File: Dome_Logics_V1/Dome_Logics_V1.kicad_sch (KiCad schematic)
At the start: 26 parts, among them J1 USB_B_Micro, J12 SERIAL_FU, J2 Conn_01x04, J3 Front Logics, J5 12OUT, J7 5V OUT, SW1 SW_Push, U1 ESP32-WROOM-32D_16MB_, U2 CJ2301_S1, U3 ME6211C33M5G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

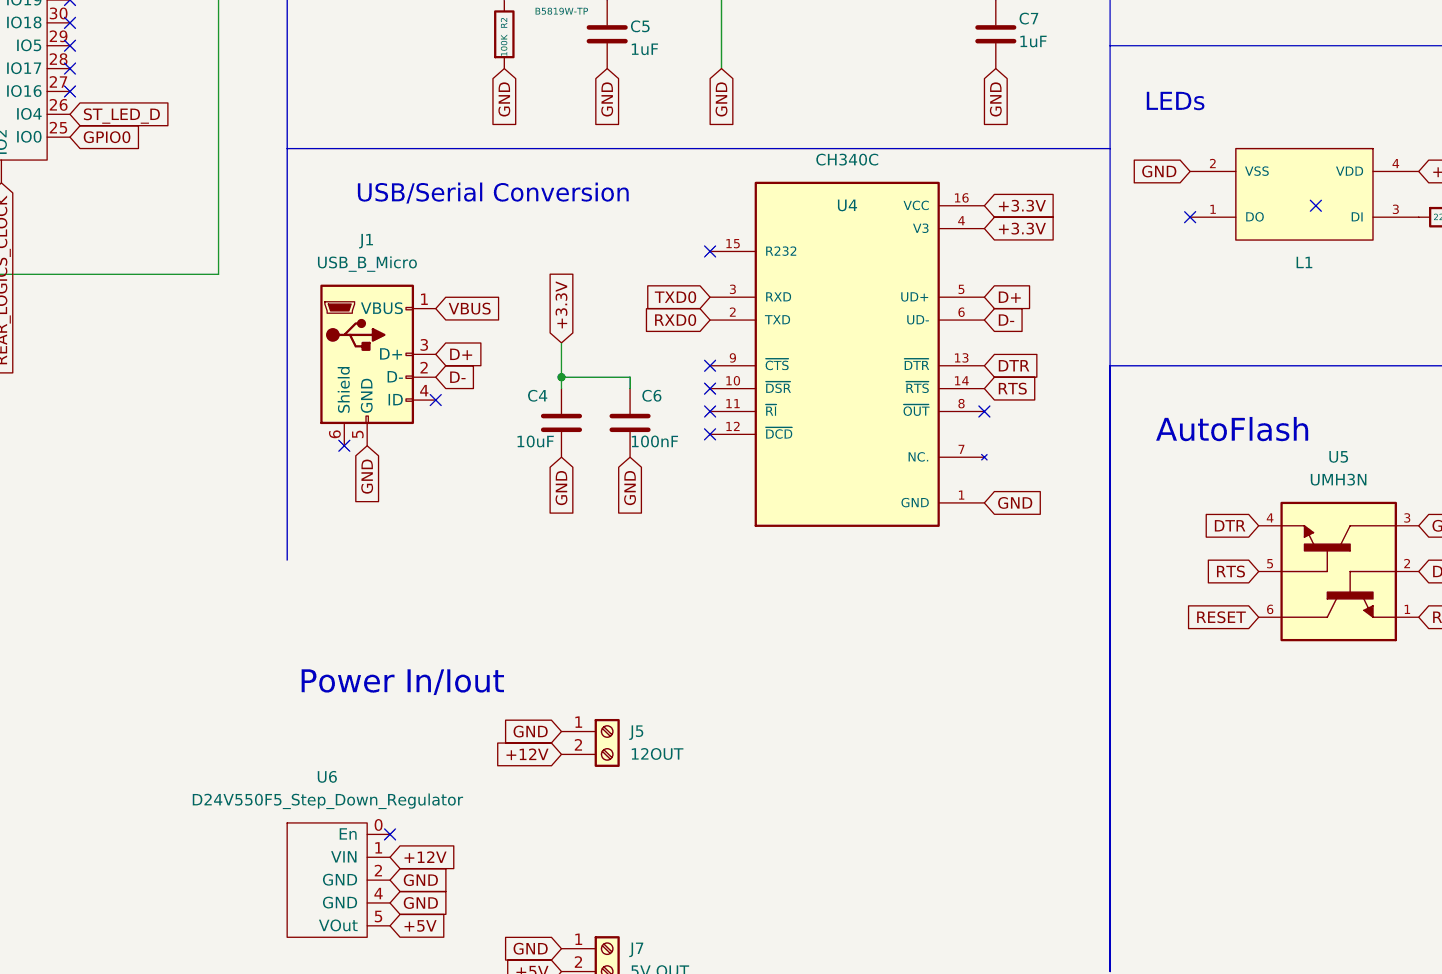
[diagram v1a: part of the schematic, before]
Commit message: added LED PCBs
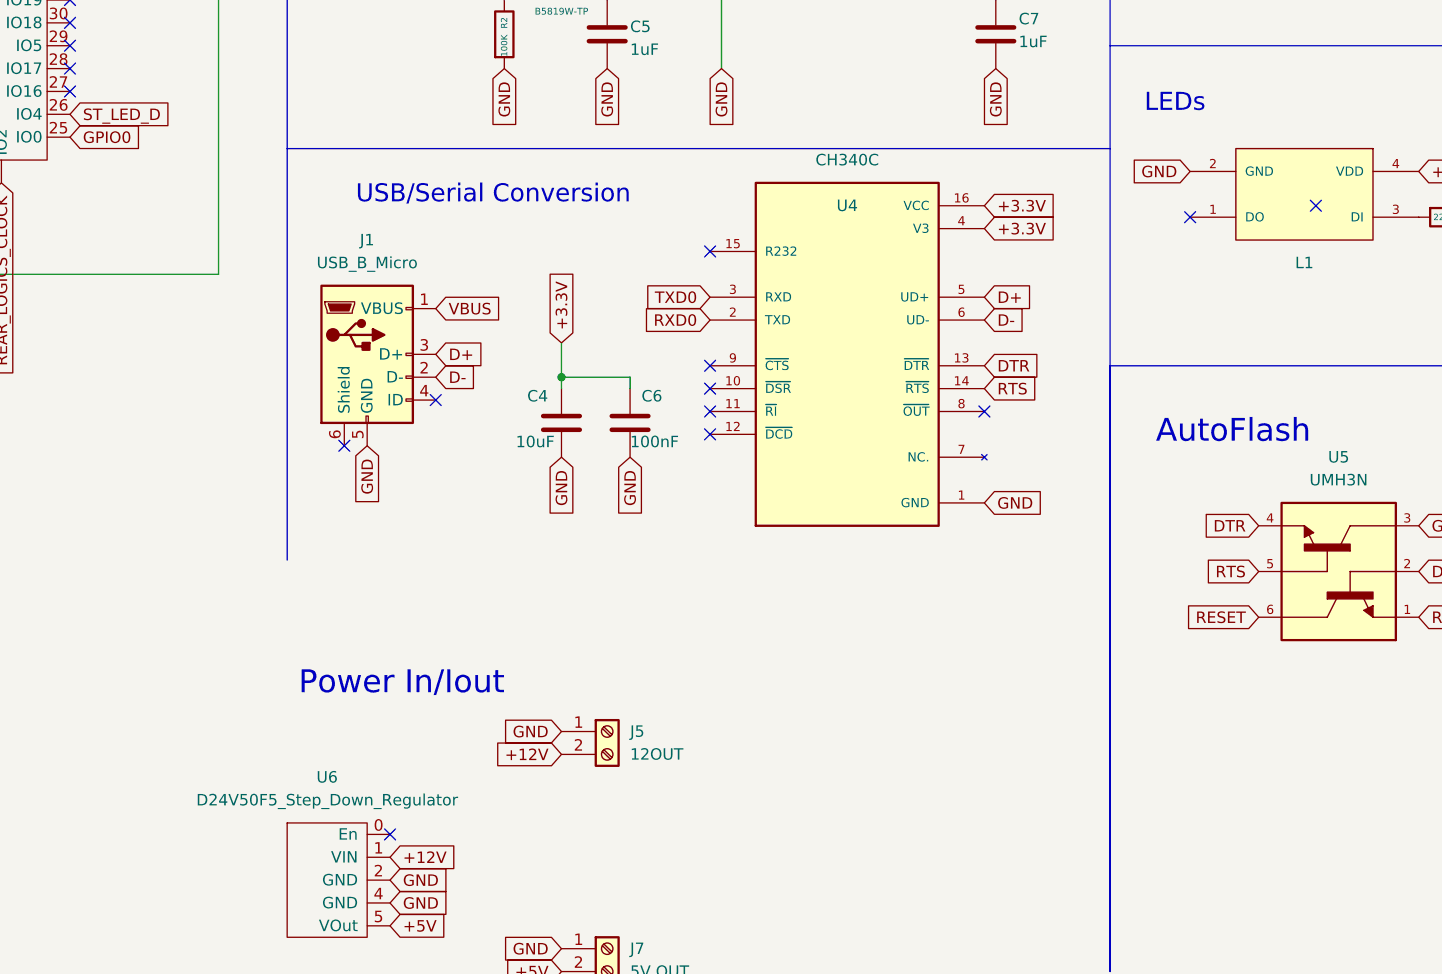
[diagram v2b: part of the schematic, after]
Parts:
- J2: LCSC (none) -> C240840
- L1: footprint Custom:WS2812B-2020 -> WS2812B-2020
- U6: value D24V550F5_Step_Down_Regulator -> D24V50F5_Step_Down_Regulator
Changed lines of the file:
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@@
       (effects (font (size 1.27 1.27)) hide)
     )
-    (property "Datasheet" "~" (id 3) (at 154.94 158.75 0)
+    (property "Datasheet" "https://datasheet.lcsc.com/lcsc/2001160007_Cixi-Kefa-Elec-KF350-3-5-2P_C474892.pdf" (id 3) (at 154.94 158.75 0)
       (effects (font (size 1.27 1.27)) hide)
     )
@@
       (effects (font (size 1.27 1.27)) hide)
     )
-    (property "Datasheet" "" (id 3) (at 181.61 55.88 0)
+    (property "Datasheet" "https://datasheet.lcsc.com/lcsc/1811131510_MICRONE-Nanjing-Micro-One-Elec-ME6211C33M5G-N_C82942.pdf" (id 3) (at 181.61 55.88 0)
       (effects (font (size 1.27 1.27)) hide)
     )
@@
       (effects (font (size 1.27 1.27)) hide)
     )
-    (property "Datasheet" "" (id 3) (at 74.93 53.34 0)
+    (property "Datasheet" "https://datasheet.lcsc.com/lcsc/2005211207_Espressif-Systems-ESP32-WROOM-32D-N16_C529578.pdf" (id 3) (at 74.93 53.34 0)
       (effects (font (size 1.27 1.27)) hide)
     )
@@
       (effects (font (size 1.27 1.27)) hide)
     )
-    (property "Datasheet" "~" (id 3) (at 154.94 134.62 0)
+    (property "Datasheet" "https://datasheet.lcsc.com/lcsc/2001160007_Cixi-Kefa-Elec-KF350-3-5-2P_C474892.pdf" (id 3) (at 154.94 134.62 0)
       (effects (font (size 1.27 1.27)) hide)
     )
@@
       (effects (font (size 1.27 1.27)) hide)
     )
-    (property "Datasheet" "" (id 3) (at 139.7 41.91 0)
+    (property "Datasheet" "https://datasheet.lcsc.com/lcsc/1809141711_Jiangsu-Changjing-Electronics-Technology-Co---Ltd--CJ2301-S1_C8547.pdf" (id 3) (at 139.7 41.91 0)
       (effects (font (size 1.27 1.27)) hide)
     )
@@
       (effects (font (size 1.27 1.27)) hide)
     )
-    (property "Datasheet" "~" (id 3) (at 132.08 93.98 0)
+    (property "Datasheet" "https://datasheet.lcsc.com/lcsc/1811131822_Amphenol-ICC-10118194-0001LF_C132563.pdf" (id 3) (at 132.08 93.98 0)
       (effects (font (size 1.27 1.27)) hide)
     )
@@
       (effects (font (size 1.27 1.27)) hide)
     )
-    (property "Datasheet" "~" (id 3) (at 154.94 57.15 0)
+    (property "Datasheet" "https://datasheet.lcsc.com/lcsc/1811081616_Murata-Electronics-GRM155R61E105KA12D_C77009.pdf" (id 3) (at 154.94 57.15 0)
       (effects (font (size 1.27 1.27)) hide)
     )
@@
       (effects (font (size 1.27 1.27)) hide)
     )
-    (property "Datasheet" "~" (id 3) (at 241.3 34.29 0)
+    (property "Datasheet" "https://datasheet.lcsc.com/lcsc/1811051309_MOLEX-470531000_C240840.pdf" (id 3) (at 241.3 34.29 0)
+      (effects (font (size 1.27 1.27)) hide)
+    )
+    (property "LCSC" "C240840" (id 4) (at 241.3 34.29 0)
       (effects (font (size 1.27 1.27)) hide)
     )
@@
       (effects (font (size 1.27 1.27)) hide)
     )
-    (property "Datasheet" "~" (id 3) (at 40.64 86.36 0)
+    (property "Datasheet" "https://datasheet.lcsc.com/lcsc/1810191222_Samsung-Electro-Mechanics-CL05B104KB54PNC_C307331.pdf" (id 3) (at 40.64 86.36 0)
       (effects (font (size 1.27 1.27)) hide)
     )
@@
       (effects (font (size 1.27 1.27)) (justify left bottom) hide)
     )
-    (property "Footprint" "Custom:WS2812B-2020" (id 2) (at 232.41 74.93 0)
-      (effects (font (size 1.27 1.27)) (justify left bottom) hide)
-    )
-    (property "Datasheet" "" (id 3) (at 232.41 74.93 0)
+    (property "Footprint" "WS2812B-2020" (id 2) (at 232.41 74.93 0)
+      (effects (font (size 1.27 1.27)) (justify left bottom) hide)
+    )
+    (property "Datasheet" "https://datasheet.lcsc.com/lcsc/2012110135_Worldsemi-WS2812B-2020_C965555.pdf" (id 3) (at 232.41 74.93 0)
       (effects (font (size 1.27 1.27)) (justify left bottom) hide)
     )
@@
       (effects (font (size 1.27 1.27)) hide)
     )
-    (property "Datasheet" "~" (id 3) (at 157.48 100.33 0)
+    (property "Datasheet" "https://datasheet.lcsc.com/lcsc/1810191222_Samsung-Electro-Mechanics-CL05B104KB54PNC_C307331.pdf" (id 3) (at 157.48 100.33 0)
       (effects (font (size 1.27 1.27)) hide)
     )
@@
       (effects (font (size 1.27 1.27)) hide)
     )
-    (property "Datasheet" "~" (id 3) (at 266.7 46.99 0)
+    (property "Datasheet" "https://datasheet.lcsc.com/lcsc/1912230932_MOLEX-22272031_C471416.pdf" (id 3) (at 266.7 46.99 0)
       (effects (font (size 1.27 1.27)) hide)
     )
@@
       (effects (font (size 1.27 1.27)) hide)
     )
-    (property "Datasheet" "~" (id 3) (at 198.12 57.15 0)
+    (property "Datasheet" "https://datasheet.lcsc.com/lcsc/1811081616_Murata-Electronics-GRM155R61E105KA12D_C77009.pdf" (id 3) (at 198.12 57.15 0)
       (effects (font (size 1.27 1.27)) hide)
     )
@@
       (effects (font (size 1.27 1.27)) (justify left bottom) hide)
     )
-    (property "Datasheet" "" (id 3) (at 234.95 111.76 0)
+    (property "Datasheet" "https://datasheet.lcsc.com/lcsc/1809211024_Jiangsu-Changjing-Electronics-Technology-Co---Ltd--UMH3N_C62892.pdf" (id 3) (at 234.95 111.76 0)
       (effects (font (size 1.27 1.27)) (justify left bottom) hide)
     )
@@
       (effects (font (size 1.27 1.27)) hide)
     )
-    (property "Datasheet" "~" (id 3) (at 143.51 57.15 0)
+    (property "Datasheet" "https://datasheet.lcsc.com/lcsc/2206010045_UNI-ROYAL-Uniroyal-Elec-0603WAF1003T5E_C25803.pdf" (id 3) (at 143.51 57.15 0)
       (effects (font (size 1.27 1.27)) hide)
     )
@@
     (in_bom yes) (on_board yes) (fields_autoplaced)
     (property "Reference" "U6" (id 0) (at 123.825 139.7 0))
-    (property "Value" "D24V550F5_Step_Down_Regulator" (id 1) (at 123.825 142.24 0))
+    (property "Value" "D24V50F5_Step_Down_Regulator" (id 1) (at 123.825 142.24 0))
     (property "Footprint" "Pololu:VoltageREG_2851" (id 2) (at 124.46 151.13 0)
       (effects (font (size 1.27 1.27)) hide)
     )
-    (property "Datasheet" "" (id 3) (at 124.46 151.13 0)
+    (property "Datasheet" "https://www.pololu.com/product/2851/specs" (id 3) (at 124.46 151.13 0)
       (effects (font (size 1.27 1.27)) hide)
     )
@@
       (effects (font (size 1.27 1.27)) hide)
     )
-    (property "Datasheet" "~" (id 3) (at 267.97 27.94 0)
+    (property "Datasheet" "https://datasheet.lcsc.com/lcsc/1912230932_MOLEX-22272031_C471416.pdf" (id 3) (at 267.97 27.94 0)
       (effects (font (size 1.27 1.27)) hide)
     )
@@
       (effects (font (size 1.27 1.27)) hide)
     )
-    (property "Datasheet" "~" (id 3) (at 33.02 50.8 0)
+    (property "Datasheet" "https://datasheet.lcsc.com/lcsc/2110111130_XKB-Connectivity-TS-1101S-B-B-B-W-A_C692465.pdf" (id 3) (at 33.02 50.8 0)
       (effects (font (size 1.27 1.27)) hide)
     )
@@
       (effects (font (size 1.27 1.27)) hide)
     )
-    (property "Datasheet" "~" (id 3) (at 31.75 86.36 0)
+    (property "Datasheet" "https://datasheet.lcsc.com/lcsc/2007131004_Samsung-Electro-Mechanics-CL05A106MP5NUNC_C315248.pdf" (id 3) (at 31.75 86.36 0)
       (effects (font (size 1.27 1.27)) hide)
     )
@@
       (effects (font (size 1.27 1.27)) hide)
     )
-    (property "Datasheet" "~" (id 3) (at 26.67 52.07 0)
+    (property "Datasheet" "https://datasheet.lcsc.com/lcsc/1810191222_Samsung-Electro-Mechanics-CL05B104KB54PNC_C307331.pdf" (id 3) (at 26.67 52.07 0)
       (effects (font (size 1.27 1.27)) hide)
     )
@@
       (effects (font (size 1.27 1.27)) hide)
     )
-    (property "Datasheet" "~" (id 3) (at 38.1 34.29 0)
+    (property "Datasheet" "https://datasheet.lcsc.com/lcsc/1811101830_TyoHM-RMC-0603-10K-F-N_C269701.pdf" (id 3) (at 38.1 34.29 0)
       (effects (font (size 1.27 1.27)) hide)
     )
@@
       (effects (font (size 1.524 1.524)) hide)
     )
-    (property "Datasheet" "" (id 3) (at 144.78 50.8 0)
-      (effects (font (size 1.524 1.524)))
+    (property "Datasheet" "https://datasheet.lcsc.com/lcsc/1810010311_MCC-Micro-Commercial-Components-B5819W-TP_C84354.pdf" (id 3) (at 144.78 50.8 0)
+      (effects (font (size 1.524 1.524)) hide)
     )
     (property "LCSC" "C84354" (id 4) (at 144.78 50.8 0)
@@
       (effects (font (size 1.27 1.27)) hide)
     )
-    (property "Datasheet" "~" (id 3) (at 162.56 48.26 0)
+    (property "Datasheet" "https://datasheet.lcsc.com/lcsc/2206010045_UNI-ROYAL-Uniroyal-Elec-0603WAF1003T5E_C25803.pdf" (id 3) (at 162.56 48.26 0)
       (effects (font (size 1.27 1.27)) hide)
     )
@@
       (effects (font (size 1.27 1.27)) (justify left bottom) hide)
     )
-    (property "Datasheet" "" (id 3) (at 181.61 93.98 0)
+    (property "Datasheet" "https://datasheet.lcsc.com/lcsc/2008191806_WCH-Jiangsu-Qin-Heng-CH340C_C84681.pdf" (id 3) (at 181.61 93.98 0)
       (effects (font (size 1.27 1.27)) (justify left bottom) hide)
     )
@@
       (effects (font (size 1.27 1.27)) hide)
     )
-    (property "Datasheet" "~" (id 3) (at 149.86 100.33 0)
+    (property "Datasheet" "https://datasheet.lcsc.com/lcsc/2007131004_Samsung-Electro-Mechanics-CL05A106MP5NUNC_C315248.pdf" (id 3) (at 149.86 100.33 0)
       (effects (font (size 1.27 1.27)) hide)
     )
@@
     )
     (path "/352b947b-2e30-436f-a33b-c4d45389f7e5"
-      (reference "L1") (unit 1) (value "WS2812B-2020") (footprint "Custom:WS2812B-2020")
+      (reference "L1") (unit 1) (value "WS2812B-2020") (footprint "WS2812B-2020")
     )
     (path "/e64c3073-694a-4368-8652-5a6e7a2016cb"
@@
     )
     (path "/6a6c41ba-5f73-451d-a447-71595c56cbc6"
-      (reference "U6") (unit 1) (value "D24V550F5_Step_Down_Regulator") (footprint "Pololu:VoltageREG_2851")
-    )
-  )
+      (reference "U6") (unit 1) (value "D24V50F5_Step_Down_Regulator") (footprint "Pololu:VoltageREG_2851")
+    )
+  )
